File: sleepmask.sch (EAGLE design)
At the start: 1 part

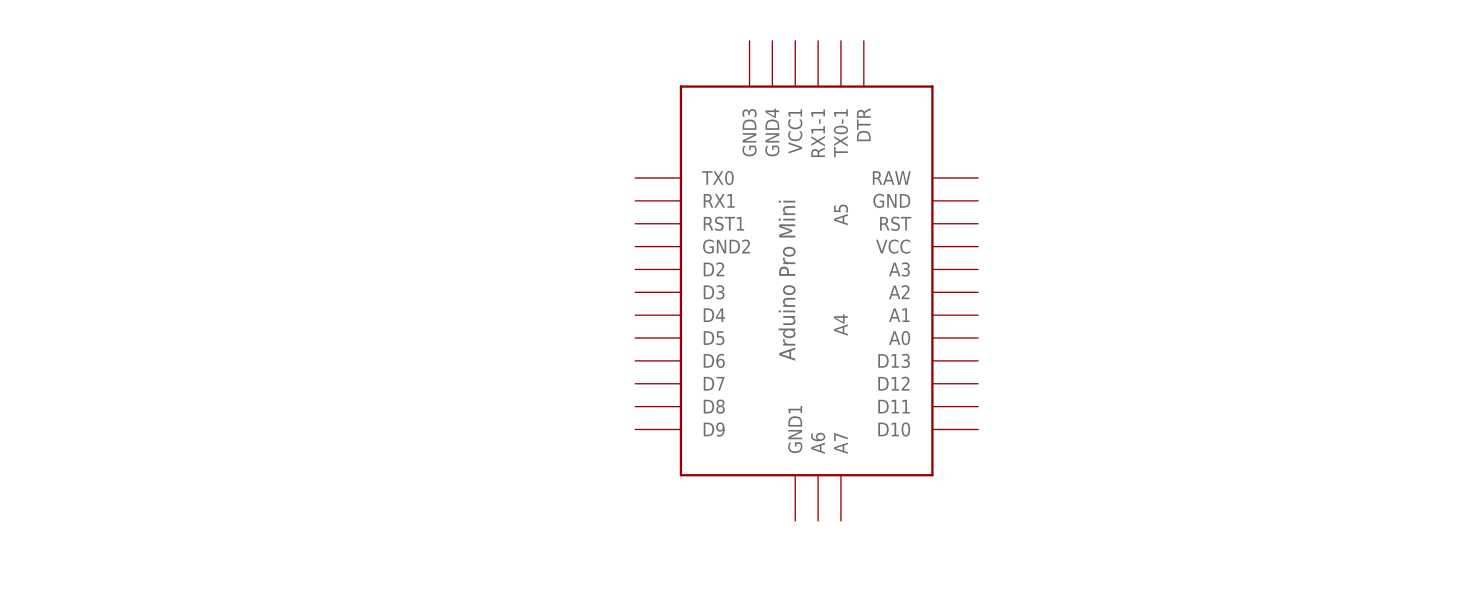
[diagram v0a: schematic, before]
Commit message: finish initial design of lighting system
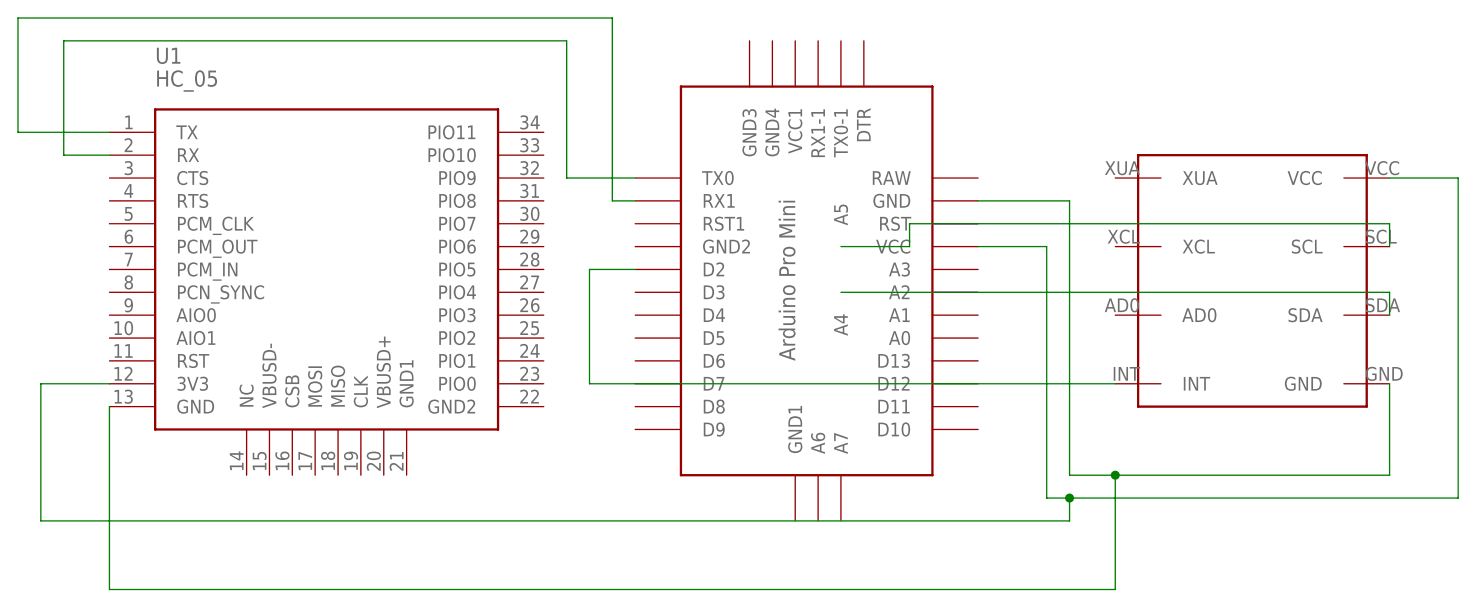
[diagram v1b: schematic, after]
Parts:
- added U$2: MPU-6050, MPU6050:MPU-6050
- added U1: HC_05, Bluetooth HC-05:HC_05
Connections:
- new net N$1: U$1.VCC, U$2.VCC, U1.3V3
- new net N$2: U$1.GND, U$2.GND, U1.GND
- new net N$3: U$1.A5, U$2.SCL
- new net N$4: U$1.A4, U$2.SDA
- new net N$5: U$1.D2, U$2.INT
- new net N$8: U$1.RX1, U1.TX
- new net N$9: U$1.TX0, U1.RX
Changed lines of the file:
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@@
 <layers>
 <layer number="1" name="Top" color="4" fill="1" visible="no" active="no"/>
+<layer number="2" name="Route2" color="1" fill="3" visible="no" active="no"/>
+<layer number="3" name="Route3" color="4" fill="3" visible="no" active="no"/>
+<layer number="4" name="Route4" color="1" fill="4" visible="no" active="no"/>
+<layer number="5" name="Route5" color="4" fill="4" visible="no" active="no"/>
+<layer number="6" name="Route6" color="1" fill="8" visible="no" active="no"/>
+<layer number="7" name="Route7" color="4" fill="8" visible="no" active="no"/>
+<layer number="8" name="Route8" color="1" fill="2" visible="no" active="no"/>
+<layer number="9" name="Route9" color="4" fill="2" visible="no" active="no"/>
+<layer number="10" name="Route10" color="1" fill="7" visible="no" active="no"/>
+<layer number="11" name="Route11" color="4" fill="7" visible="no" active="no"/>
+<layer number="12" name="Route12" color="1" fill="5" visible="no" active="no"/>
+<layer number="13" name="Route13" color="4" fill="5" visible="no" active="no"/>
+<layer number="14" name="Route14" color="1" fill="6" visible="no" active="no"/>
+<layer number="15" name="Route15" color="4" fill="6" visible="no" active="no"/>
 <layer number="16" name="Bottom" color="1" fill="1" visible="no" active="no"/>
 <layer number="17" name="Pads" color="2" fill="1" visible="no" active="no"/>
@@
 <layer number="48" name="Document" color="7" fill="1" visible="no" active="no"/>
 <layer number="49" name="Reference" color="7" fill="1" visible="no" active="no"/>
+<layer number="50" name="dxf" color="7" fill="1" visible="no" active="no"/>
 <layer number="51" name="tDocu" color="7" fill="1" visible="no" active="no"/>
 <layer number="52" name="bDocu" color="7" fill="1" visible="no" active="no"/>
+<layer number="53" name="tGND_GNDA" color="7" fill="9" visible="no" active="no"/>
+<layer number="54" name="bGND_GNDA" color="1" fill="9" visible="no" active="no"/>
+<layer number="56" name="wert" color="7" fill="1" visible="no" active="no"/>
 <layer number="88" name="SimResults" color="9" fill="1" visible="yes" active="yes"/>
 <layer number="89" name="SimProbes" color="9" fill="1" visible="yes" active="yes"/>
@@
 <layer number="97" name="Info" color="7" fill="1" visible="yes" active="yes"/>
 <layer number="98" name="Guide" color="6" fill="1" visible="yes" active="yes"/>
+<layer number="100" name="Muster" color="7" fill="1" visible="no" active="no"/>
+<layer number="101" name="Patch_Top" color="12" fill="4" visible="yes" active="yes"/>
+<layer number="102" name="Vscore" color="7" fill="1" visible="yes" active="yes"/>
+<layer number="104" name="Name" color="7" fill="1" visible="yes" active="yes"/>
+<layer number="116" name="Patch_BOT" color="9" fill="4" visible="yes" active="yes"/>
+<layer number="121" name="_tsilk" color="7" fill="1" visible="yes" active="yes"/>
+<layer number="122" name="_bsilk" color="7" fill="1" visible="yes" active="yes"/>
+<layer number="151" name="HeatSink" color="7" fill="1" visible="yes" active="yes"/>
+<layer number="200" name="200bmp" color="1" fill="10" visible="no" active="no"/>
+<layer number="201" name="201bmp" color="2" fill="1" visible="no" active="no"/>
+<layer number="202" name="202bmp" color="3" fill="1" visible="no" active="no"/>
+<layer number="250" name="Descript" color="3" fill="1" visible="no" active="no"/>
+<layer number="251" name="SMDround" color="12" fill="11" visible="no" active="no"/>
+<layer number="254" name="cooling" color="7" fill="1" visible="yes" active="yes"/>
 </layers>
 <schematic xreflabel="%F%N/%S.%C%R" xrefpart="/%S.%C%R">
@@
 <parts>
 <part name="U$1" library="Arduino-clone" deviceset="ABK-PRO-MINI" device=""/>
+<part name="U$2" library="MPU6050" deviceset="MPU-6050" device=""/>
+<part name="U1" library="Bluetooth HC-05" deviceset="HC_05" device=""/>
 </parts>
 <sheets>
@@
 <instances>
 <instance part="U$1" gate="G$1" x="71.12" y="45.72"/>
+<instance part="U$2" gate="G$1" x="116.84" y="48.26"/>
+<instance part="U1" gate="G$1" x="12.7" y="48.26"/>
 </instances>
 <busses>
 </busses>
 <nets>
+<net name="N$1" class="0">
+<segment>
+<pinref part="U$2" gate="G$1" pin="VCC"/>
+<wire x1="132.08" y1="58.42" x2="139.7" y2="58.42" width="0.1524" layer="91"/>
+<wire x1="139.7" y1="58.42" x2="139.7" y2="22.86" width="0.1524" layer="91"/>
+<wire x1="139.7" y1="22.86" x2="96.52" y2="22.86" width="0.1524" layer="91"/>
+<wire x1="96.52" y1="22.86" x2="93.98" y2="22.86" width="0.1524" layer="91"/>
+<wire x1="93.98" y1="22.86" x2="93.98" y2="50.8" width="0.1524" layer="91"/>
+<pinref part="U$1" gate="G$1" pin="VCC"/>
+<wire x1="93.98" y1="50.8" x2="86.36" y2="50.8" width="0.1524" layer="91"/>
+<pinref part="U1" gate="G$1" pin="3V3"/>
+<wire x1="-10.16" y1="35.56" x2="-17.78" y2="35.56" width="0.1524" layer="91"/>
+<wire x1="-17.78" y1="35.56" x2="-17.78" y2="20.32" width="0.1524" layer="91"/>
+<wire x1="-17.78" y1="20.32" x2="96.52" y2="20.32" width="0.1524" layer="91"/>
+<wire x1="96.52" y1="22.86" x2="96.52" y2="20.32" width="0.1524" layer="91"/>
+<junction x="96.52" y="22.86"/>
+</segment>
+</net>
+<net name="N$2" class="0">
+<segment>
+<pinref part="U$2" gate="G$1" pin="GND"/>
+<wire x1="132.08" y1="35.56" x2="132.08" y2="25.4" width="0.1524" layer="91"/>
+<wire x1="132.08" y1="25.4" x2="101.6" y2="25.4" width="0.1524" layer="91"/>
+<wire x1="101.6" y1="25.4" x2="96.52" y2="25.4" width="0.1524" layer="91"/>
+<wire x1="96.52" y1="25.4" x2="96.52" y2="55.88" width="0.1524" layer="91"/>
+<pinref part="U$1" gate="G$1" pin="GND"/>
+<wire x1="96.52" y1="55.88" x2="86.36" y2="55.88" width="0.1524" layer="91"/>
+<pinref part="U1" gate="G$1" pin="GND"/>
+<wire x1="-10.16" y1="33.02" x2="-10.16" y2="12.7" width="0.1524" layer="91"/>
+<wire x1="-10.16" y1="12.7" x2="101.6" y2="12.7" width="0.1524" layer="91"/>
+<wire x1="101.6" y1="12.7" x2="101.6" y2="25.4" width="0.1524" layer="91"/>
+<junction x="101.6" y="25.4"/>
+</segment>
+</net>
+<net name="N$3" class="0">
+<segment>
+<pinref part="U$1" gate="G$1" pin="A5"/>
+<wire x1="71.12" y1="50.8" x2="78.74" y2="50.8" width="0.1524" layer="91"/>
+<wire x1="78.74" y1="50.8" x2="78.74" y2="53.34" width="0.1524" layer="91"/>
+<wire x1="78.74" y1="53.34" x2="132.08" y2="53.34" width="0.1524" layer="91"/>
+<pinref part="U$2" gate="G$1" pin="SCL"/>
+<wire x1="132.08" y1="53.34" x2="132.08" y2="50.8" width="0.1524" layer="91"/>
+</segment>
+</net>
+<net name="N$4" class="0">
+<segment>
+<pinref part="U$1" gate="G$1" pin="A4"/>
+<wire x1="71.12" y1="45.72" x2="132.08" y2="45.72" width="0.1524" layer="91"/>
+<pinref part="U$2" gate="G$1" pin="SDA"/>
+<wire x1="132.08" y1="45.72" x2="132.08" y2="43.18" width="0.1524" layer="91"/>
+</segment>
+</net>
+<net name="N$5" class="0">
+<segment>
+<pinref part="U$2" gate="G$1" pin="INT"/>
+<wire x1="101.6" y1="35.56" x2="43.18" y2="35.56" width="0.1524" layer="91"/>
+<wire x1="43.18" y1="35.56" x2="43.18" y2="48.26" width="0.1524" layer="91"/>
+<pinref part="U$1" gate="G$1" pin="D2"/>
+<wire x1="43.18" y1="48.26" x2="48.26" y2="48.26" width="0.1524" layer="91"/>
+</segment>
+</net>
+<net name="N$8" class="0">
+<segment>
+<pinref part="U1" gate="G$1" pin="TX"/>
+<wire x1="-10.16" y1="63.5" x2="-20.32" y2="63.5" width="0.1524" layer="91"/>
+<wire x1="-20.32" y1="63.5" x2="-20.32" y2="76.2" width="0.1524" layer="91"/>
+<wire x1="-20.32" y1="76.2" x2="45.72" y2="76.2" width="0.1524" layer="91"/>
+<wire x1="45.72" y1="76.2" x2="45.72" y2="55.88" width="0.1524" layer="91"/>
+<pinref part="U$1" gate="G$1" pin="RX1"/>
+<wire x1="45.72" y1="55.88" x2="48.26" y2="55.88" width="0.1524" layer="91"/>
+</segment>
+</net>
+<net name="N$9" class="0">
+<segment>
+<pinref part="U$1" gate="G$1" pin="TX0"/>
+<wire x1="48.26" y1="58.42" x2="40.64" y2="58.42" width="0.1524" layer="91"/>
+<wire x1="40.64" y1="58.42" x2="40.64" y2="73.66" width="0.1524" layer="91"/>
+<wire x1="40.64" y1="73.66" x2="-15.24" y2="73.66" width="0.1524" layer="91"/>
+<wire x1="-15.24" y1="73.66" x2="-15.24" y2="60.96" width="0.1524" layer="91"/>
+<pinref part="U1" gate="G$1" pin="RX"/>
+<wire x1="-15.24" y1="60.96" x2="-10.16" y2="60.96" width="0.1524" layer="91"/>
+</segment>
+</net>
 </nets>
 </sheet>
